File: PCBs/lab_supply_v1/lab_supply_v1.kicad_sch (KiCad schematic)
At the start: 1 part, among them J1 LINE-IN

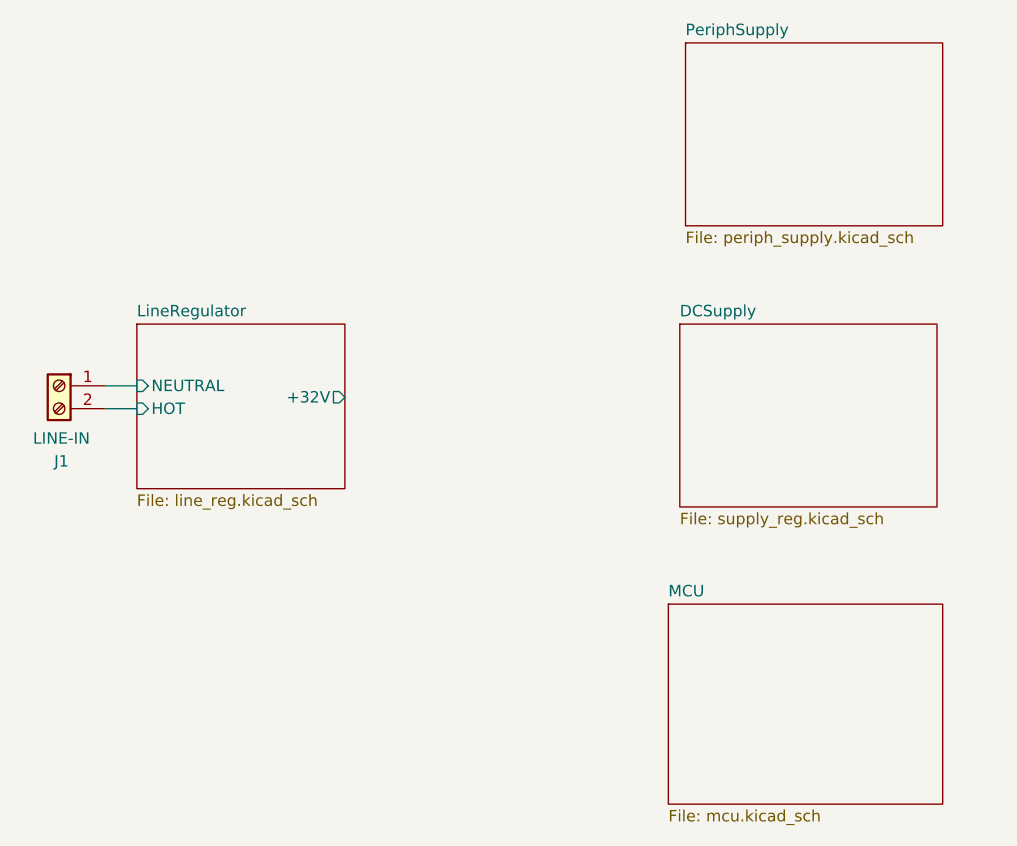
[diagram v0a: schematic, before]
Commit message: Updated PCB added current sense buffer added ADC/DAC for current/voltage sensing added ACDC converter bypass made optimal supply voltage 36 V @ 5 A
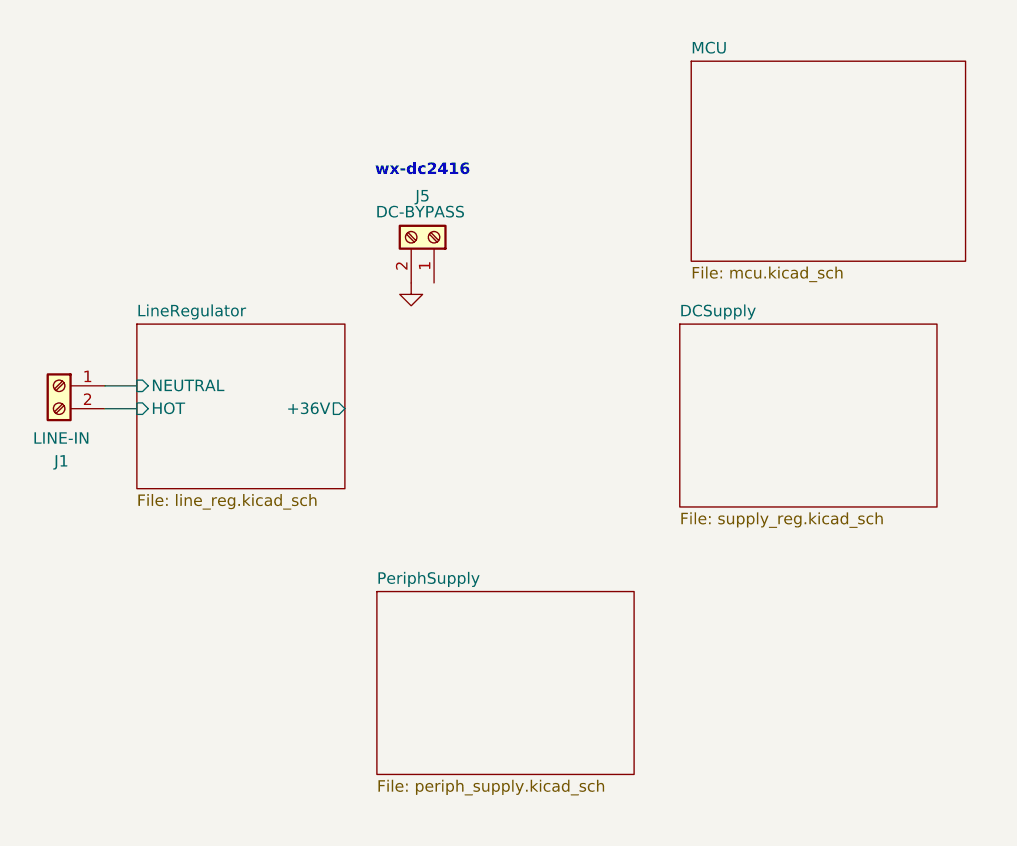
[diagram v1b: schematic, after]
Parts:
- added J5: DC-BYPASS, symbol Connector:Screw_Terminal_01x02
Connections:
- new net GND: J5.2 (Pin_2)
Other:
- sheet LineRegulator ports: added +36V; removed +32V
- note added: "wx-dc2416"
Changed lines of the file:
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@@
+		)
+	)
+	(text "wx-dc2416"
+		(exclude_from_sim no)
+		(at 125.73 49.784 0)
+		(effects
+			(font
+				(size 1.27 1.27)
+				(thickness 0.254)
+				(bold yes)
+			)
+		)
+	)
+	(symbol
+		(lib_id "power:GND")
+		(at 124.46 62.23 0)
+		(unit 1)
+		(exclude_from_sim no)
+		(in_bom yes)
+		(on_board yes)
+		(dnp no)
+		(fields_autoplaced yes)
+		(property "Reference" "#PWR021"
+			(at 124.46 68.58 0)
+			(effects
+				(font
+					(size 1.27 1.27)
+				)
+				(hide yes)
+			)
+		)
+		(property "Value" "GND"
+			(at 124.46 67.31 0)
+			(effects
+				(font
+					(size 1.27 1.27)
+				)
+				(hide yes)
+			)
+		)
+		(property "Footprint" ""
+			(at 124.46 62.23 0)
+			(effects
+				(font
+					(size 1.27 1.27)
+				)
+				(hide yes)
+			)
+		)
+		(property "Datasheet" ""
+			(at 124.46 62.23 0)
+			(effects
+				(font
+					(size 1.27 1.27)
+				)
+				(hide yes)
+			)
+		)
+		(property "Description" "Power symbol creates a global label with name \"GND\" , ground"
+			(at 124.46 62.23 0)
+			(effects
+				(font
+					(size 1.27 1.27)
+				)
+				(hide yes)
+			)
+		)
+		(pin "1"
+		)
+		(instances
+			(project "lab_supply_v1"
+				(path "/c381ddef-a21e-4847-9921-7e6cff5e49a3"
+					(reference "#PWR021")
+					(unit 1)
+				)
+			)
+		)
+	)
+	(symbol
+		(lib_id "Connector:Screw_Terminal_01x02")
+		(at 127 57.15 270)
+		(mirror x)
+		(unit 1)
+		(exclude_from_sim no)
+		(in_bom yes)
+		(on_board yes)
+		(dnp no)
+		(property "Reference" "J5"
+			(at 125.73 52.578 90)
+			(effects
+				(font
+					(size 1.27 1.27)
+				)
+			)
+		)
+		(property "Value" "DC-BYPASS"
+			(at 125.476 54.356 90)
+			(effects
+				(font
+					(size 1.27 1.27)
+				)
+			)
+		)
+		(property "Footprint" ""
+			(at 127 57.15 0)
+			(effects
+				(font
+					(size 1.27 1.27)
+				)
+				(hide yes)
+			)
+		)
+		(property "Datasheet" "~"
+			(at 127 57.15 0)
+			(effects
+				(font
+					(size 1.27 1.27)
+				)
+				(hide yes)
+			)
+		)
+		(property "Description" "Generic screw terminal, single row, 01x02, script generated (kicad-library-utils/schlib/autogen/connector/)"
+			(at 127 57.15 0)
+			(effects
+				(font
+					(size 1.27 1.27)
+				)
+				(hide yes)
+			)
+		)
+		(pin "1"
+		)
+		(pin "2"
+		)
+		(instances
+			(project "lab_supply_v1"
+				(path "/c381ddef-a21e-4847-9921-7e6cff5e49a3"
+					(reference "J5")
+					(unit 1)
+				)
+			)
 		)
 	)
@@
 	)
 	(sheet
-		(at 153.035 97.917)
+		(at 155.575 37.592)
 		(size 30.48 22.225)
 		(fields_autoplaced yes)
@@
 		)
 		(property "Sheetname" "MCU"
-			(at 153.035 97.2054 0)
+			(at 155.575 36.8804 0)
 			(effects
 				(font
@@
 		)
 		(property "Sheetfile" "mcu.kicad_sch"
-			(at 153.035 120.7266 0)
+			(at 155.575 60.4016 0)
 			(effects
 				(font
@@
 	)
 	(sheet
-		(at 154.94 35.56)
+		(at 120.65 96.52)
 		(size 28.575 20.32)
 		(fields_autoplaced yes)
@@
 		)
 		(property "Sheetname" "PeriphSupply"
-			(at 154.94 34.8484 0)
+			(at 120.65 95.8084 0)
 			(effects
 				(font
@@
 		)
 		(property "Sheetfile" "periph_supply.kicad_sch"
-			(at 154.94 56.4646 0)
+			(at 120.65 117.4246 0)
 			(effects
 				(font
@@
 			)
 		)
-		(pin "+32V" output
-			(at 117.094 74.93 0)
-			(effects
-				(font
+		(pin "+36V" output
+			(at 117.094 76.2 0)
+			(effects
+				(font

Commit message: Updated PCB began dynamic load work
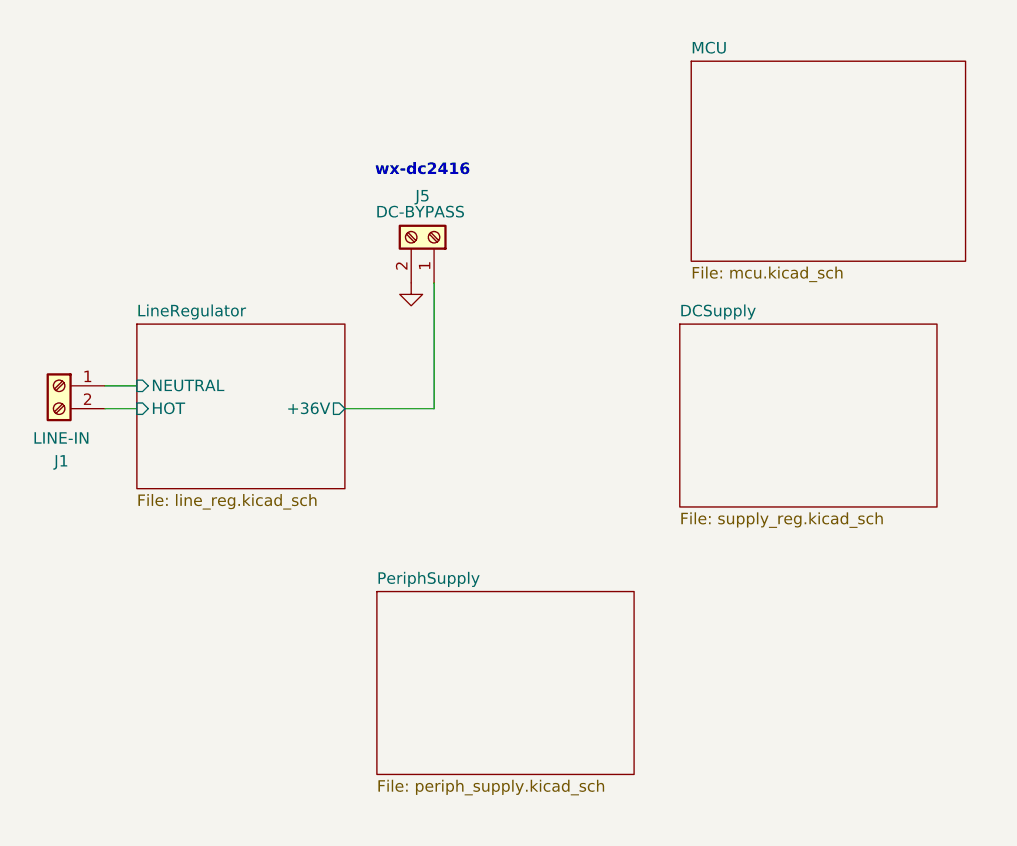
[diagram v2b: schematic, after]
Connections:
- net LineRegulator/+36V: now also J5.1 (Pin_1)
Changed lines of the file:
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@@
+	(wire
+		(pts
+			(xy 127 62.23) (xy 127 76.2)
+		)
+		(stroke
+			(width 0)
+			(type default)
+		)
+	)
 	(wire
 		(pts
@@
 		)
 		(stroke
+			(width 0)
+			(type default)
+		)
+	)
+	(wire
+		(pts
+			(xy 117.094 76.2) (xy 127 76.2)
+		)
+		(stroke
